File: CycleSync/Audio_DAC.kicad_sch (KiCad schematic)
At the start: 20 parts, among them U5 PCM5102A

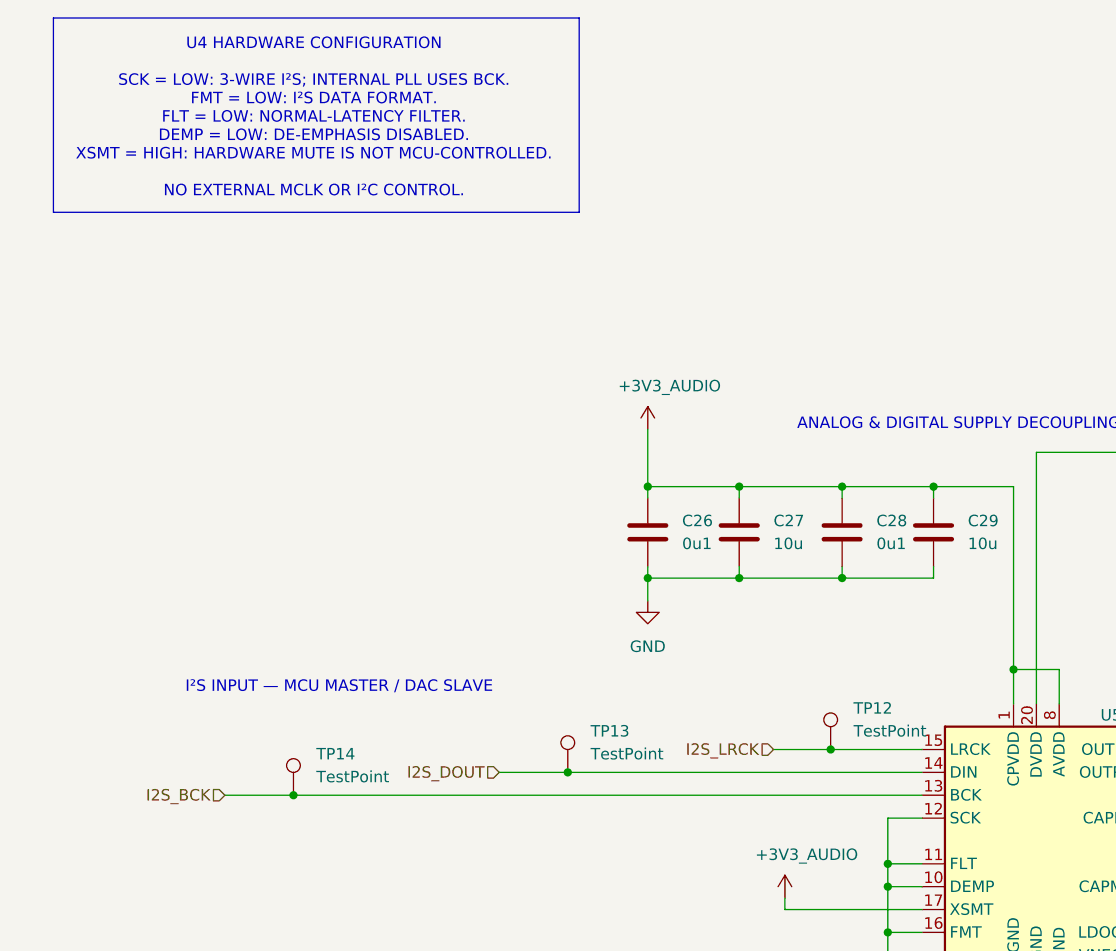
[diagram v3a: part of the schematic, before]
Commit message: added some new testpoints for I2C
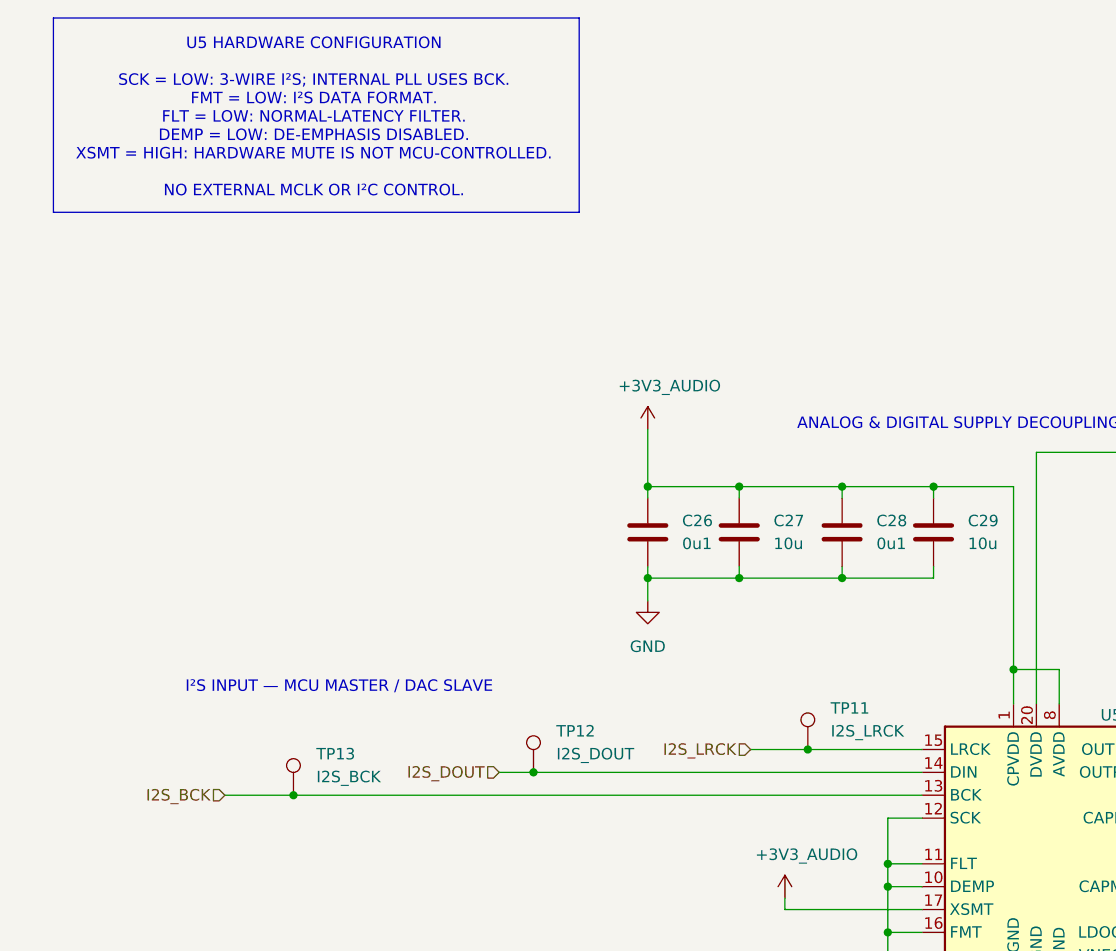
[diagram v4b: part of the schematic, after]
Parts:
- C26, C28, C30, C35, C36, C38: footprint (none) -> Capacitor_SMD:C_0402_1005Metric
- C27, C29, C31, C34, C37, C39: footprint (none) -> Capacitor_SMD:C_0805_2012Metric
- C32, C33: footprint (none) -> Capacitor_SMD:C_0603_1608Metric
- R25, R26: footprint (none) -> Resistor_SMD:R_0402_1005Metric
- TP11: renamed from TP12; value TestPoint -> I2S_LRCK; footprint (none) -> TestPoint:TestPoint_Pad_D1.5mm
- TP12: renamed from TP13; value TestPoint -> I2S_DOUT; footprint (none) -> TestPoint:TestPoint_Pad_D1.5mm
- TP13: renamed from TP14; value TestPoint -> I2S_BCK; footprint (none) -> TestPoint:TestPoint_Pad_D1.5mm
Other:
- note added: "U5 HARDWARE CONFIGURATION SCK = LOW: 3-WIRE I²S; INTERNAL PLL USES BCK. FMT = LOW: I²S DATA FORMAT. FLT = LOW: NORMAL-LATENCY FILTER. DEMP = LOW: DE-EMPHASIS DISABLED. XSMT = HIGH: HARDWARE MUTE IS NOT MCU-CONTROLLED. NO EXTERNAL MCLK OR I²C CONTROL."
- note removed: "U4 HARDWARE CONFIGURATION SCK = LOW: 3-WIRE I²S; INTERNAL PLL USES BCK. FMT = LOW: I²S DATA FORMAT. FLT = LOW: NORMAL-LATENCY FILTER. DEMP = LOW: DE-EMPHASIS DISABLED. XSMT = HIGH: HARDWARE MUTE IS NOT MCU-CONTROLLED. NO EXTERNAL MCLK OR I²C CONTROL."
- moved on the sheet: TP11, TP12
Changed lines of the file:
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@@
 		)
 	)
-	(text "U4 HARDWARE CONFIGURATION\n\nSCK = LOW: 3-WIRE I²S; INTERNAL PLL USES BCK.\nFMT = LOW: I²S DATA FORMAT.\nFLT = LOW: NORMAL-LATENCY FILTER.\nDEMP = LOW: DE-EMPHASIS DISABLED.\nXSMT = HIGH: HARDWARE MUTE IS NOT MCU-CONTROLLED.\n\nNO EXTERNAL MCLK OR I²C CONTROL."
+	(text "U5 HARDWARE CONFIGURATION\n\nSCK = LOW: 3-WIRE I²S; INTERNAL PLL USES BCK.\nFMT = LOW: I²S DATA FORMAT.\nFLT = LOW: NORMAL-LATENCY FILTER.\nDEMP = LOW: DE-EMPHASIS DISABLED.\nXSMT = HIGH: HARDWARE MUTE IS NOT MCU-CONTROLLED.\n\nNO EXTERNAL MCLK OR I²C CONTROL."
 		(exclude_from_sim no)
 		(at 44.196 30.226 0)
@@
 	)
 	(junction
-		(at 72.39 102.87)
-		(diameter 0)
-		(color 0 0 0 0)
-	)
-	(junction
 		(at 171.45 118.11)
 		(diameter 0)
@@
 	)
 	(junction
+		(at 99.06 100.33)
+		(diameter 0)
+		(color 0 0 0 0)
+	)
+	(junction
 		(at 200.66 109.22)
 		(diameter 0)
@@
 	)
 	(junction
+		(at 68.58 102.87)
+		(diameter 0)
+		(color 0 0 0 0)
+	)
+	(junction
 		(at 124.46 133.35)
 		(diameter 0)
@@
 		(color 0 0 0 0)
 	)
-	(junction
-		(at 101.6 100.33)
-		(diameter 0)
-		(color 0 0 0 0)
-	)
 	(wire
 		(pts
@@
 	(wire
 		(pts
-			(xy 121.92 133.35) (xy 124.46 133.35)
+			(xy 99.06 100.33) (xy 111.76 100.33)
 		)
 		(stroke
@@
 	(wire
 		(pts
-			(xy 176.53 128.27) (xy 181.61 128.27)
+			(xy 121.92 133.35) (xy 124.46 133.35)
 		)
 		(stroke
@@
 	(wire
 		(pts
-			(xy 107.95 115.57) (xy 111.76 115.57)
+			(xy 176.53 128.27) (xy 181.61 128.27)
 		)
 		(stroke
@@
 	(wire
 		(pts
-			(xy 121.92 128.27) (xy 121.92 133.35)
+			(xy 107.95 115.57) (xy 111.76 115.57)
 		)
 		(stroke
@@
 	(wire
 		(pts
-			(xy 81.28 81.28) (xy 81.28 80.01)
+			(xy 121.92 128.27) (xy 121.92 133.35)
 		)
 		(stroke
@@
 	(wire
 		(pts
-			(xy 101.6 100.33) (xy 111.76 100.33)
+			(xy 81.28 81.28) (xy 81.28 80.01)
 		)
 		(stroke
@@
 	(wire
 		(pts
-			(xy 64.77 102.87) (xy 72.39 102.87)
+			(xy 64.77 102.87) (xy 68.58 102.87)
 		)
 		(stroke
@@
 	(wire
 		(pts
-			(xy 95.25 100.33) (xy 101.6 100.33)
+			(xy 92.71 100.33) (xy 99.06 100.33)
 		)
 		(stroke
@@
 	(wire
 		(pts
-			(xy 127 91.44) (xy 127 95.25)
+			(xy 68.58 102.87) (xy 111.76 102.87)
 		)
 		(stroke
@@
 	(wire
 		(pts
-			(xy 171.45 118.11) (xy 181.61 118.11)
+			(xy 127 91.44) (xy 127 95.25)
 		)
 		(stroke
@@
 	(wire
 		(pts
-			(xy 111.76 120.65) (xy 107.95 120.65)
+			(xy 171.45 118.11) (xy 181.61 118.11)
 		)
 		(stroke
@@
 	(wire
 		(pts
-			(xy 102.87 81.28) (xy 113.03 81.28)
+			(xy 111.76 120.65) (xy 107.95 120.65)
 		)
 		(stroke
@@
 	(wire
 		(pts
-			(xy 143.51 120.65) (xy 143.51 118.11)
+			(xy 102.87 81.28) (xy 113.03 81.28)
 		)
 		(stroke
@@
 	(wire
 		(pts
-			(xy 139.7 67.31) (xy 149.86 67.31)
+			(xy 143.51 120.65) (xy 143.51 118.11)
 		)
 		(stroke
@@
 	(wire
 		(pts
-			(xy 139.7 77.47) (xy 139.7 76.2)
+			(xy 139.7 67.31) (xy 149.86 67.31)
 		)
 		(stroke
@@
 	(wire
 		(pts
-			(xy 72.39 102.87) (xy 111.76 102.87)
+			(xy 139.7 77.47) (xy 139.7 76.2)
 		)
 		(stroke
@@
 	(hierarchical_label "I2S_LRCK"
 		(shape input)
-		(at 95.25 100.33 180)
+		(at 92.71 100.33 180)
 		(effects
 			(font
@@
 	(symbol
 		(lib_id "Connector:TestPoint")
-		(at 72.39 102.87 0)
+		(at 68.58 102.87 0)
 		(unit 1)
 		(body_style 1)
@@
 		(dnp no)
 		(fields_autoplaced yes)
-		(property "Reference" "TP13"
-			(at 74.93 98.2979 0)
+		(property "Reference" "TP12"
+			(at 71.12 98.2979 0)
 			(show_name no)
 			(do_not_autoplace no)
@@
 			)
 		)
-		(property "Value" "TestPoint"
-			(at 74.93 100.8379 0)
+		(property "Value" "I2S_DOUT"
+			(at 71.12 100.8379 0)
 			(show_name no)
 			(do_not_autoplace no)
@@
 			)
 		)
-		(property "Footprint" ""
-			(at 77.47 102.87 0)
+		(property "Footprint" "TestPoint:TestPoint_Pad_D1.5mm"
+			(at 73.66 102.87 0)
 			(hide yes)
 			(show_name no)
@@
 		)
 		(property "Datasheet" ""
-			(at 77.47 102.87 0)
+			(at 73.66 102.87 0)
 			(hide yes)
 			(show_name no)
@@
 		)
 		(property "Description" "test point"
-			(at 72.39 102.87 0)
+			(at 68.58 102.87 0)
 			(hide yes)
 			(show_name no)
@@
 			(project "CycleSync"
 				(path "/3f2cc6af-e67b-48ad-b391-ff7619611bd8/b5b9e253-8b7f-4bb9-bef8-83286ffed738"
-					(reference "TP13")
+					(reference "TP12")
 					(unit 1)
 				)
@@
 			)
 		)
-		(property "Footprint" ""
+		(property "Footprint" "Capacitor_SMD:C_0402_1005Metric"
 			(at 201.6252 119.38 0)
 			(hide yes)
@@
 			)
 		)
-		(property "Footprint" ""
+		(property "Footprint" "Capacitor_SMD:C_0805_2012Metric"
 			(at 90.4748 72.39 0)
 			(hide yes)
@@
 			)
 		)
-		(property "Footprint" ""
+		(property "Footprint" "Capacitor_SMD:C_0402_1005Metric"
 			(at 138.7348 68.58 0)
 			(hide yes)
@@
 			)
 		)
-		(property "Footprint" ""
+		(property "Footprint" "Capacitor_SMD:C_0805_2012Metric"
 			(at 219.71 108.2548 0)
 			(hide yes)
@@
 			)
 		)
-		(property "Footprint" ""
+		(property "Footprint" "Capacitor_SMD:C_0402_1005Metric"
 			(at 80.3148 72.39 0)
 			(hide yes)
@@
 			)
 		)
-		(property "Footprint" ""
+		(property "Footprint" "Resistor_SMD:R_0402_1005Metric"
 			(at 199.39 85.598 90)
 			(hide yes)
@@
 			)
 		)
-		(property "Footprint" ""
+		(property "Footprint" "Capacitor_SMD:C_0805_2012Metric"
 			(at 172.4152 128.27 0)
 			(hide yes)
@@
 			)
 		)
-		(property "Footprint" ""
+		(property "Footprint" "Capacitor_SMD:C_0603_1608Metric"
 			(at 146.05 126.6952 0)
 			(hide yes)
@@
 	(symbol
 		(lib_id "Connector:TestPoint")
-		(at 101.6 100.33 0)
+		(at 99.06 100.33 0)
 		(unit 1)
 		(body_style 1)
@@
 		(dnp no)
 		(fields_autoplaced yes)
-		(property "Reference" "TP12"
-			(at 104.14 95.7579 0)
+		(property "Reference" "TP11"
+			(at 101.6 95.7579 0)
 			(show_name no)
 			(do_not_autoplace no)
@@
 			)
 		)
-		(property "Value" "TestPoint"
-			(at 104.14 98.2979 0)
+		(property "Value" "I2S_LRCK"
+			(at 101.6 98.2979 0)
 			(show_name no)
 			(do_not_autoplace no)
@@
 			)
 		)
-		(property "Footprint" ""
-			(at 106.68 100.33 0)
+		(property "Footprint" "TestPoint:TestPoint_Pad_D1.5mm"
+			(at 104.14 100.33 0)
 			(hide yes)
 			(show_name no)
@@
 		)
 		(property "Datasheet" ""
-			(at 106.68 100.33 0)
+			(at 104.14 100.33 0)
 			(hide yes)
 			(show_name no)
@@
 		)
 		(property "Description" "test point"
-			(at 101.6 100.33 0)
+			(at 99.06 100.33 0)
 			(hide yes)
 			(show_name no)
@@
 			(project "CycleSync"
 				(path "/3f2cc6af-e67b-48ad-b391-ff7619611bd8/b5b9e253-8b7f-4bb9-bef8-83286ffed738"
-					(reference "TP12")
+					(reference "TP11")
 					(unit 1)
 				)
@@
 			)
 		)
-		(property "Footprint" ""
+		(property "Footprint" "Resistor_SMD:R_0402_1005Metric"
 			(at 181.61 110.998 90)
 			(hide yes)
@@
 			)
 		)
-		(property "Footprint" ""
+		(property "Footprint" "Capacitor_SMD:C_0402_1005Metric"
 			(at 223.2152 91.44 0)
 			(hide yes)
@@
 		(dnp no)
 		(fields_autoplaced yes)
-		(property "Reference" "TP14"
+		(property "Reference" "TP13"
 			(at 44.45 100.8379 0)
 			(show_name no)
@@
 			)
 		)
-		(property "Value" "TestPoint"
+		(property "Value" "I2S_BCK"
 			(at 44.45 103.3779 0)
 			(show_name no)
@@
 			)
 		)
-		(property "Footprint" ""
+		(property "Footprint" "TestPoint:TestPoint_Pad_D1.5mm"
 			(at 46.99 105.41 0)
 			(hide yes)
@@
 			(project "CycleSync"
 				(path "/3f2cc6af-e67b-48ad-b391-ff7619611bd8/b5b9e253-8b7f-4bb9-bef8-83286ffed738"
-					(reference "TP14")
+					(reference "TP13")
 					(unit 1)
 				)
@@
 			)
 		)
-		(property "Footprint" ""
+		(property "Footprint" "Capacitor_SMD:C_0805_2012Metric"
 			(at 240.03 82.8548 0)
 			(hide yes)
@@
 			)
 		)
-		(property "Footprint" ""
+		(property "Footprint" "Capacitor_SMD:C_0603_1608Metric"
 			(at 148.2852 115.57 0)
 			(hide yes)
@@
 			)
 		)
-		(property "Footprint" ""
+		(property "Footprint" "Capacitor_SMD:C_0402_1005Metric"
 			(at 101.9048 72.39 0)
 			(hide yes)
@@
 			)
 		)
-		(property "Footprint" ""
+		(property "Footprint" "Capacitor_SMD:C_0402_1005Metric"
 			(at 182.5752 128.27 0)
 			(hide yes)
@@
 			)
 		)
-		(property "Footprint" ""
+		(property "Footprint" "Capacitor_SMD:C_0805_2012Metric"
 			(at 148.8948 68.58 0)
 			(hide yes)
@@
 			)
 		)
-		(property "Footprint" ""
+		(property "Footprint" "Capacitor_SMD:C_0805_2012Metric"
 			(at 112.0648 72.39 0)
 			(hide yes)

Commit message: added footprints and manufacturer part number
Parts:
- added TP28: GND_DAC, TestPoint:TestPoint_Pad_D1.5mm, symbol Connector:TestPoint
- C26, C28, C30, C35: Distributor Link (none) -> https://jlcpcb.com/partdetail/291005-CL05B104KB54PNC/C307331; MANUFACTURER (none) -> Samsung Electro-Mechanics; MPN (none) -> CL05B104KB54PNC
- C27, C29, C31, C34: Distributor Link (none) -> https://jlcpcb.com/partdetail/236937-GRM21BZ71E106KE15L/C23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; MANUFACTURER (none) -> Murata Electronics; MPN (none) -> GRM21BZ71E106KE15L
- C32, C33: Distributor Link (none) -> https://jlcpcb.com/partdetail/24366-CL10A225KO8NNNC/C23630; MANUFACTURER (none) -> Samsung Electro-Mechanics; MPN (none) -> CL10A225KO8NNNC
- C36, C38: Distributor Link (none) -> https://jlcpcb.com/partdetail/KEMET-C0402C222J3GACAUTO/C184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; MANUFACTURER (none) -> KEMET; MPN (none) -> C0402C222J3GACAUTO
- C37, C39: Distributor Link (none) -> https://jlcpcb.com/partdetail/2131-CL21A475KAQNNNE/C1779; MANUFACTURER (none) -> Samsung Electro-Mechanics; MPN (none) -> CL21A475KAQNNNE
- R25, R26: Distributor Link (none) -> https://jlcpcb.com/partdetail/25860-0402WGF4700TCE/C25117; MANUFACTURER (none) -> UNI-ROYAL(Uniroyal Elec); MPN (none) -> 0402WGF4700TCE
- TP11, TP12, TP13: now left out of the parts list
- U5: value PCM5102A -> PCM5102APWR; Distributor Link (none) -> https://jlcpcb.com/partdetail/TexasInstruments-PCM5102APWR/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; MANUFACTURER (none) -> Texas Instruments; MPN (none) -> PCM5102APWR
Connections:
- net GND: now also TP28.1
